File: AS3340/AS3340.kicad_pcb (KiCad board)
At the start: 2 copper layers, 88.4 x 55.9 mm, 42 parts, among them J1 SAW_OUT, J101 SQUARE_OUT, J102 Pulse width, J2 TRIANGLE_OUT, J201 PWM CV in, J202 PWM, J3 CV in, J301 Sync switch, J4 Coarse tune, J901 Eurorack power header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

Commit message: Final stripboard and AS3340
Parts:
- added RV2: 10k, Potentiometer_THT:Potentiometer_Runtron_RM-065_Vertical, F.Cu at (85.3, 81.8)
- moved D901 10.7 mm to (90.2, 68.1), turned to 90 degrees
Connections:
- R3 pad 1: +12V -> Net-(R3-Pad1)
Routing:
- net Net-(R1-Pad2): track 18.2 -> 36.8 mm
- net Net-(R6-Pad1): track 73.8 -> 85.2 mm
- net Net-(C901-Pad1): track 27.5 -> 16.8 mm
- net +12V: track 119.3 -> 129.6 mm
- net -12V: track 84.0 -> 84.9 mm
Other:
- board text added: "JLCJLCJLCJLC"
- board text added: "NOT BOTH!!!"
- board text added: "or"

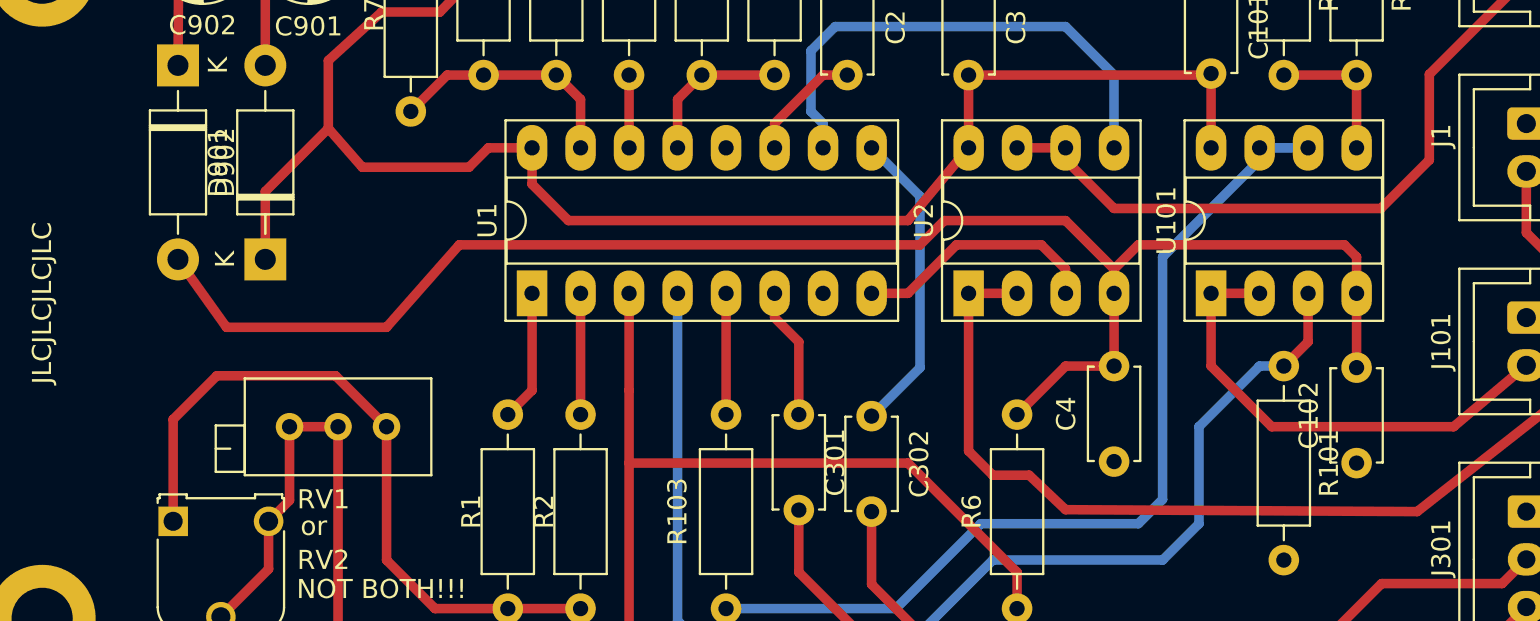
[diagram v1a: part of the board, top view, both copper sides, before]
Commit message: Corrected value. Rearranged silkscreen
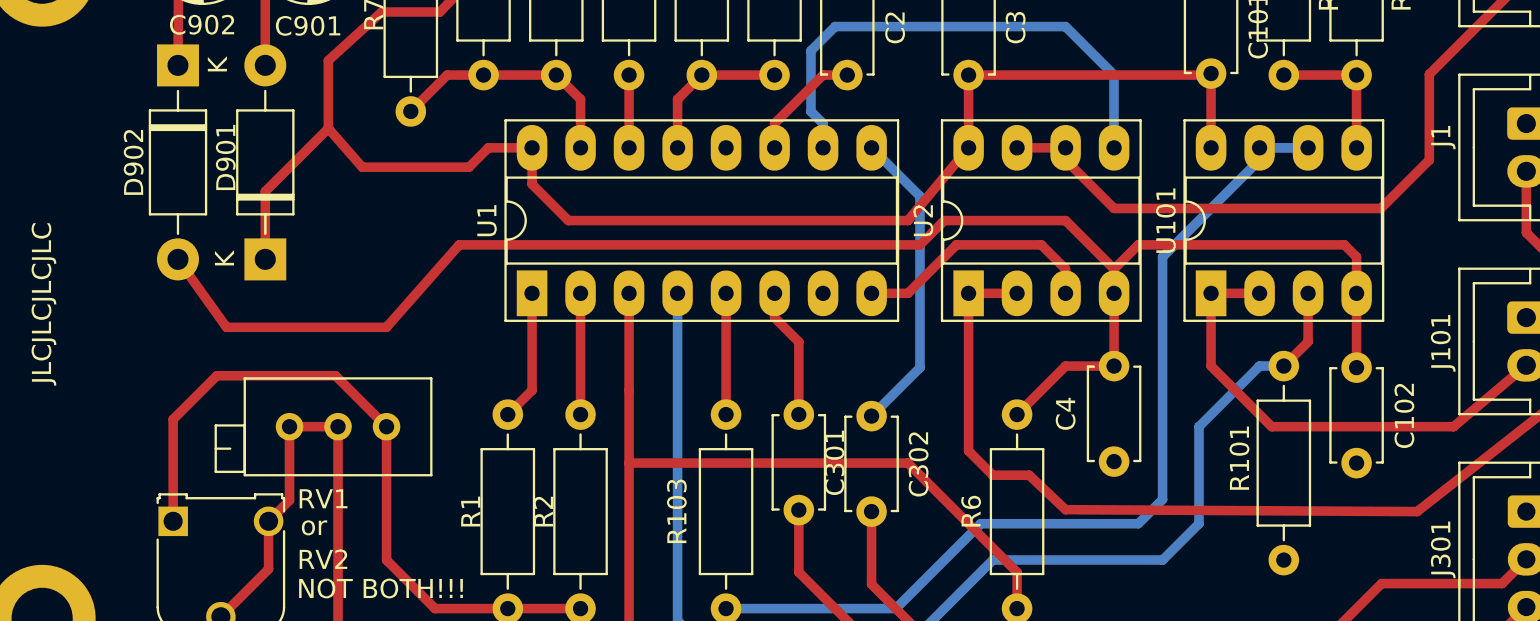
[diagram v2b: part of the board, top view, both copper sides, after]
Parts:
- C1: value 10µ -> 10n
- C2: value 1nF -> 1n

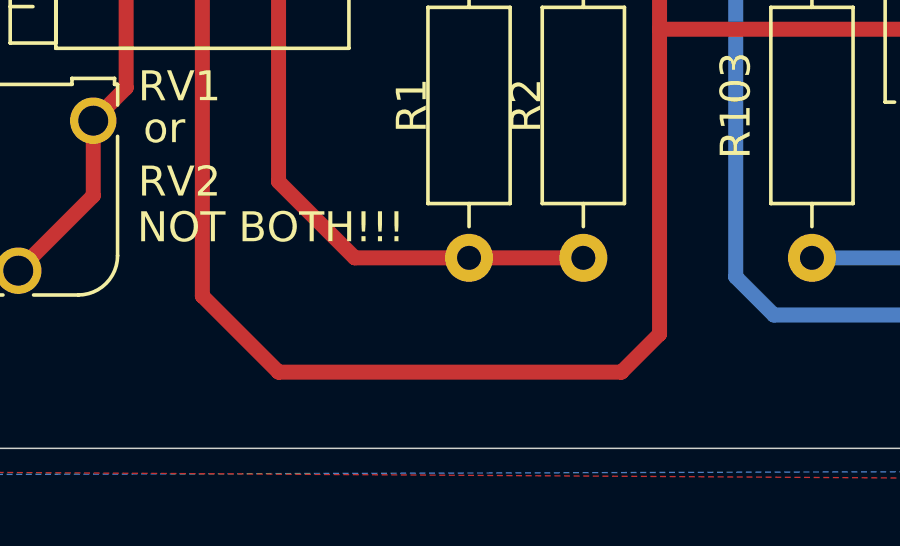
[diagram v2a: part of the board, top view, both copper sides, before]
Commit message: Corrected error in the circuit
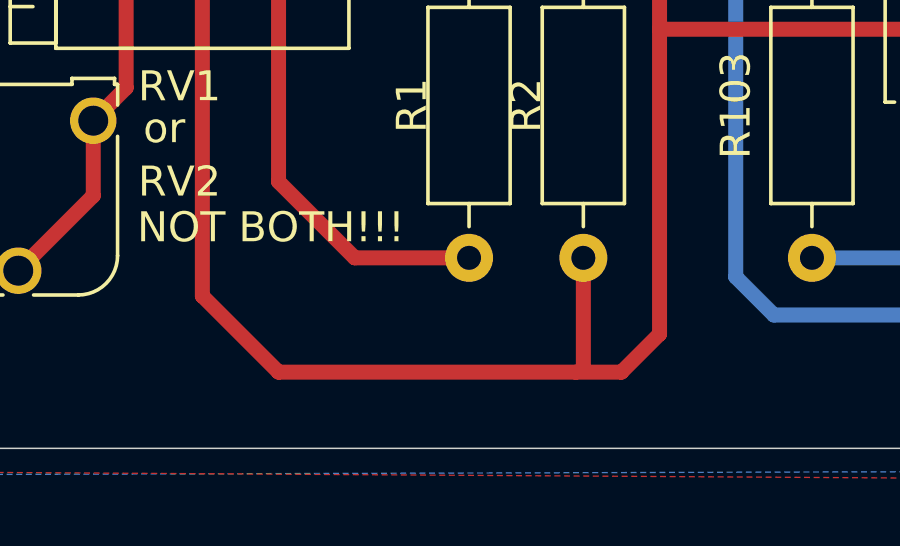
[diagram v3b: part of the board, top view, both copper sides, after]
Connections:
- R2 pad 1: Net-(R1-Pad2) -> Net-(R2-Pad1)
- R3 pad 1: Net-(R3-Pad1) -> +12V
- R6 pad 1: Net-(R6-Pad1) -> Net-(R2-Pad1)
- RV1 pad 2: Net-(R6-Pad1) -> Net-(R2-Pad1)
- RV1 pad 3: Net-(R6-Pad1) -> Net-(R2-Pad1)
- RV2 pad 2: Net-(R6-Pad1) -> Net-(R2-Pad1)
- RV2 pad 3: Net-(R6-Pad1) -> Net-(R2-Pad1)
- U1 pad 3: Net-(R6-Pad1) -> Net-(R2-Pad1)
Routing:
- net Net-(R2-Pad1): track 0.00 -> 89.2 mm
- net Net-(R6-Pad1): track 85.2 -> 0.00 mm
- net Net-(R1-Pad2): track 36.8 -> 32.9 mm
